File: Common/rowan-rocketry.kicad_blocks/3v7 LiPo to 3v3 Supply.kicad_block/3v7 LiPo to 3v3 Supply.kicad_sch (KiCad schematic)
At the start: 5 parts

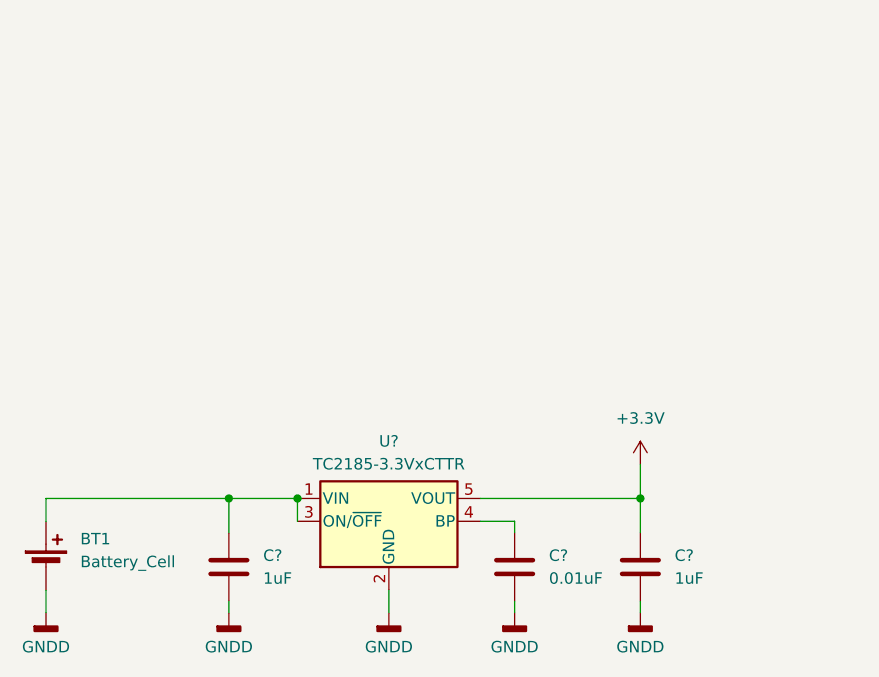
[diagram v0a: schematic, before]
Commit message: More reuse blocks. Added battery circuit to ride along board
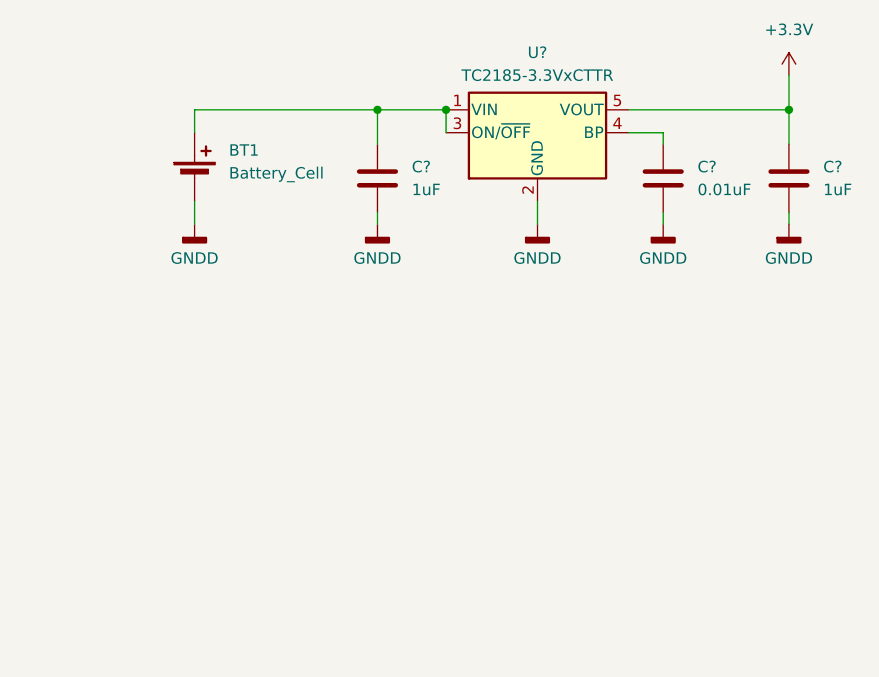
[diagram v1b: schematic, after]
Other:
- moved on the sheet: BT1, C?, U?
